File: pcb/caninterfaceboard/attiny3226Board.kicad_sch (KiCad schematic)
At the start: 78 parts, among them J1 AVR UART, J10 NTC2, J11 Attiny UDPI, J12 Flywheel, J13 1Wire, J2 CAN, J3 AVR ISP, J4 NTC3, J5 12V In, J6 FuelLevel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

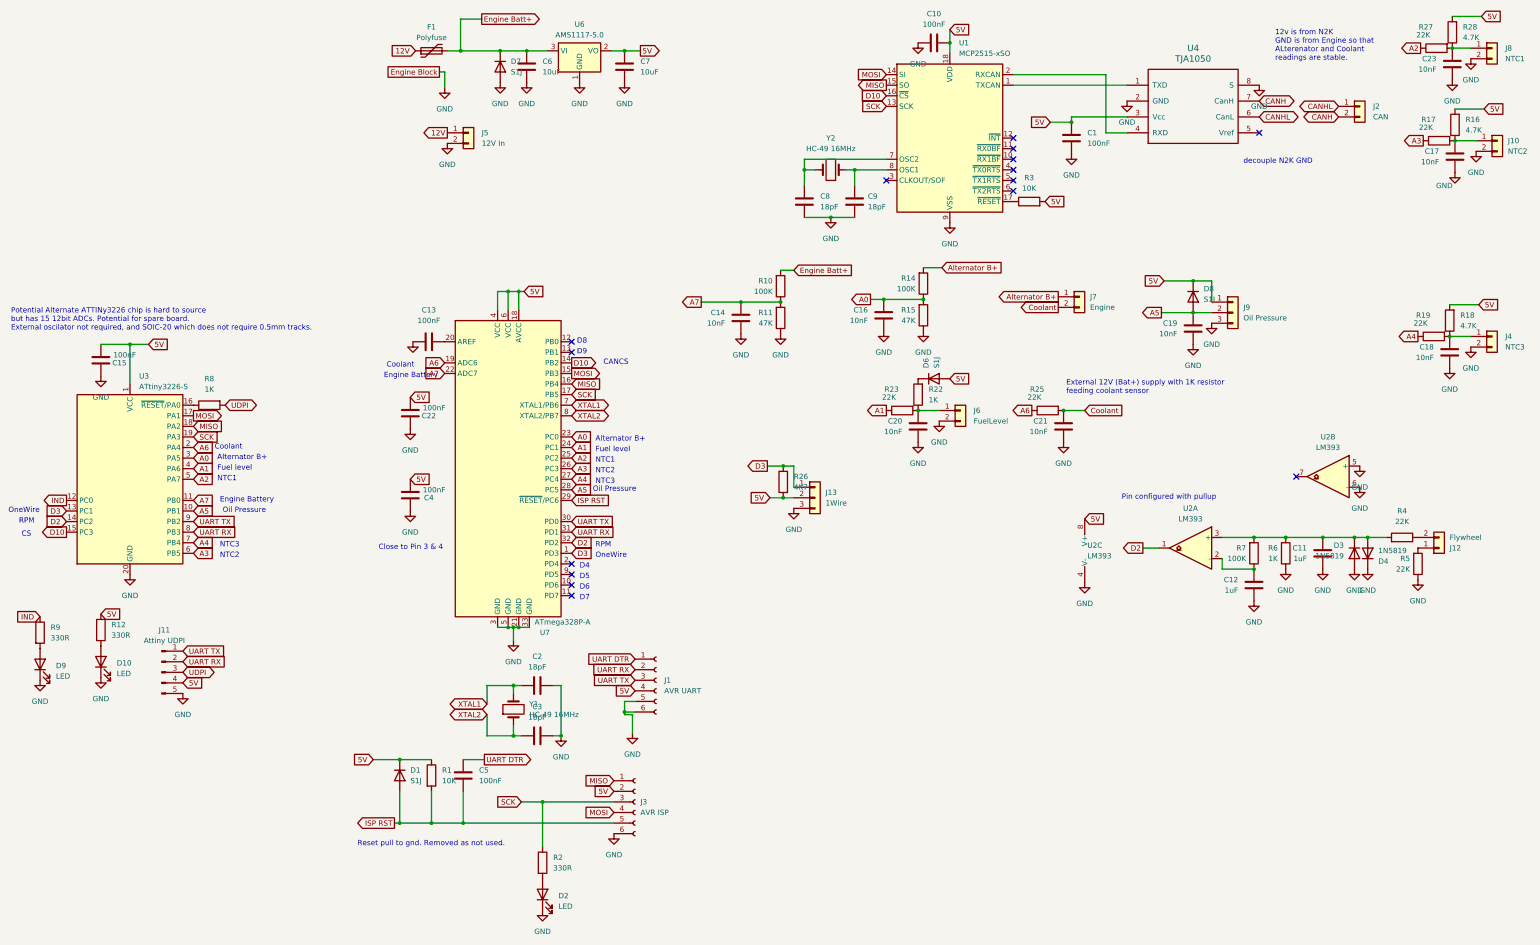
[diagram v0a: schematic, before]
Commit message: Added a attiny3226 veresion for better ADC accuracy
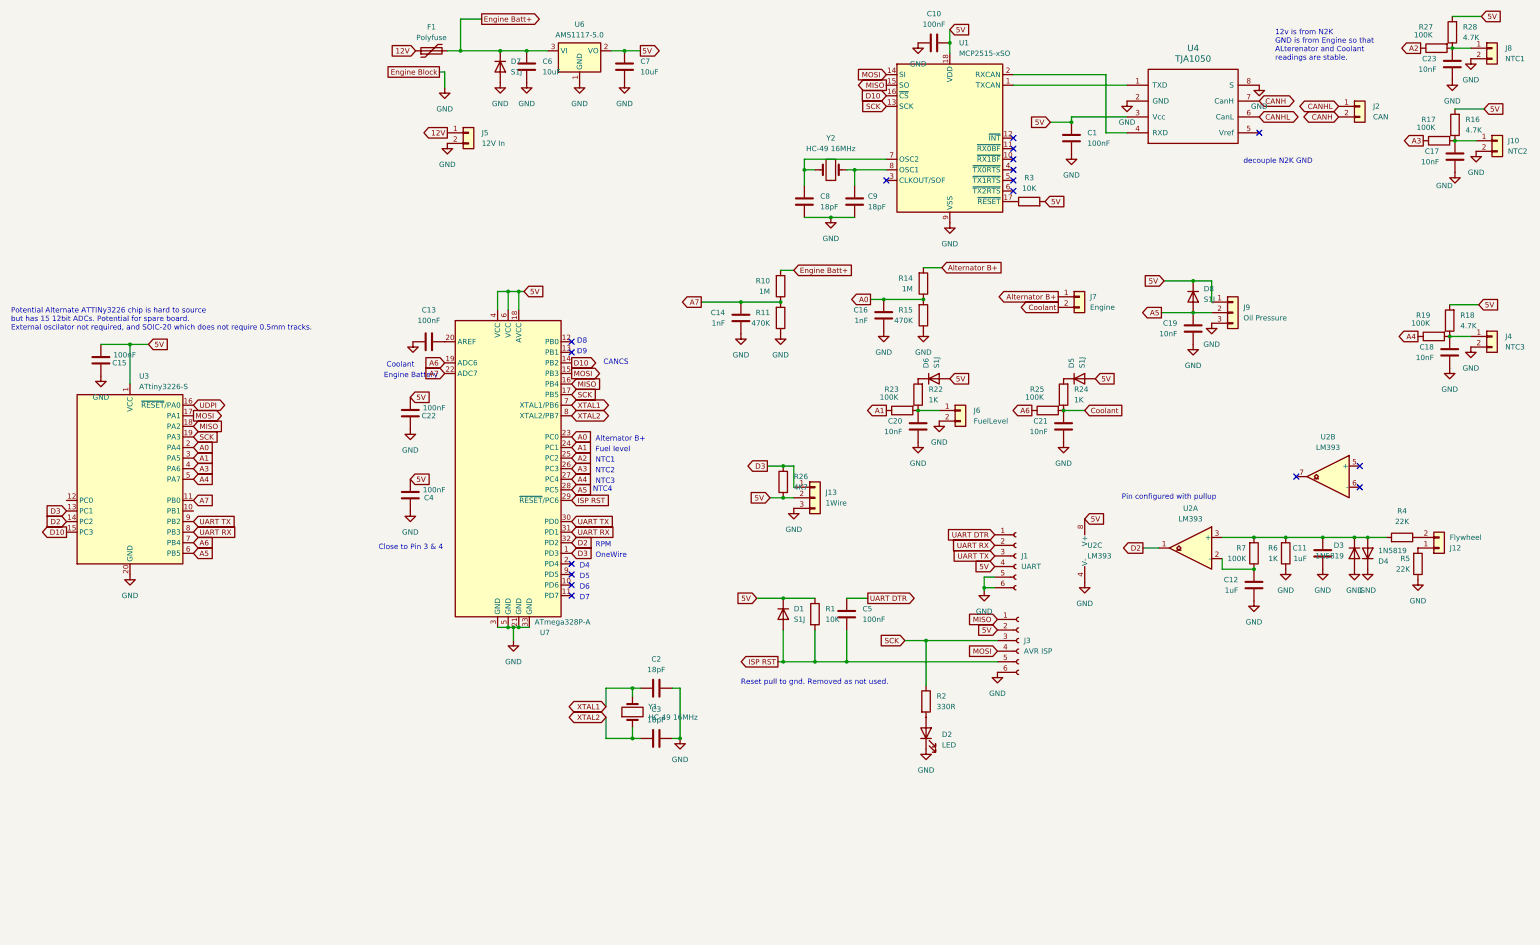
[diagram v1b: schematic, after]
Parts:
- removed D10, D9: LED, LED_SMD:LED_0805_2012Metric_Pad1.15x1.40mm_HandSolder, symbol Device:LED
- removed J11: Attiny UDPI, Connector_PinHeader_2.54mm:PinHeader_1x05_P2.54mm_Vertical, symbol Connector:Conn_01x05_Pin
- removed R12, R9: 330R, Resistor_SMD:R_0805_2012Metric_Pad1.20x1.40mm_HandSolder, symbol Device:R
- removed R8: 1K, Resistor_SMD:R_0805_2012Metric_Pad1.20x1.40mm_HandSolder, symbol Device:R
- added D5: S1J, Diode_SMD:D_0805_2012Metric_Pad1.15x1.40mm_HandSolder, symbol Device:D
- added R24: 1K, Resistor_SMD:R_0805_2012Metric_Pad1.20x1.40mm_HandSolder, symbol Device:R
- C14, C16: value 10nF -> 1nF
- J1: value AVR UART -> UART
- R10, R14: value 100K -> 1M
- R11, R15: value 47K -> 470K
- R17, R19, R23, R25, R27: value 22K -> 100K
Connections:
- net 5V: now also D5.2 (A)
- net A0: now also U3.2 (PA4); no longer U3.3 (PA5)
- net A1: now also U3.3 (PA5); no longer U3.4 (PA6)
- net A2: no longer U3.5 (PA7)
- net A3: now also U3.4 (PA6); no longer U3.6 (PB5)
- net A4: now also U3.5 (PA7); no longer U3.7 (PB4)
- net A5: now also U3.6 (PB5); no longer U3.10 (PB1)
- net A6: now also U3.7 (PB4); no longer U3.2 (PA4)
- net Coolant: now also R24.1
- net GND: no longer U2.5 (+), U2.6 (-)
- net UDPI: now also U3.16 (~{RESET}/PA0)
- net IND: no longer names the net of U3.12 (PC0)
- new net: D5.1 (K), R24.2
- no-connect marks 15 -> 17
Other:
- note added: "NTC4"
- note removed: "CS"
- note removed: "External 12V (Bat+) supply with 1K resistor feeding coolant sensor"
- note removed: "Oil Pressure"
- moved on the sheet: C2, C3, C5, D1, D2, J1, J3, R1, R2, Y1

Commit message: Finally mare the RPM to pulse amp stable
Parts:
- added C24: 100nF, Capacitor_SMD:C_0805_2012Metric_Pad1.18x1.45mm_HandSolder, symbol Device:C
- added R9: 10K, Resistor_SMD:R_0805_2012Metric_Pad1.20x1.40mm_HandSolder, symbol Device:R
- C11: value 1uF -> 470nF
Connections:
- net 5V: now also C24.2, R9.2
- net D2: now also R9.1
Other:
- note added: "Decoupling must be close to the LM393"
- note removed: "Pin configured with pullup"

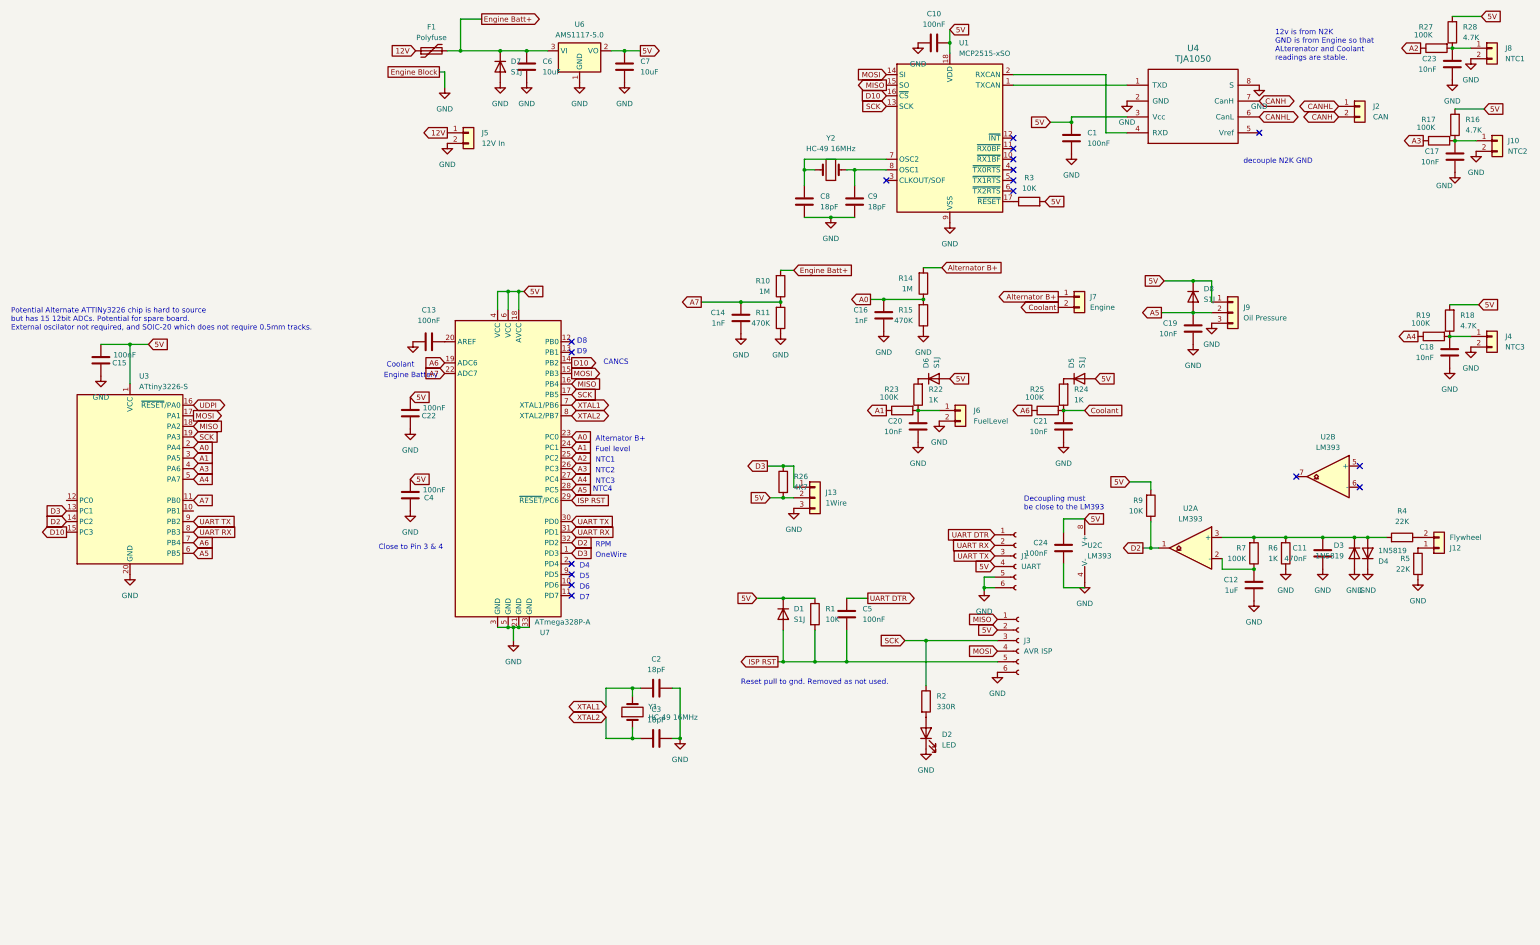
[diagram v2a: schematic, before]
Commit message: Improved flywheel detection circuit
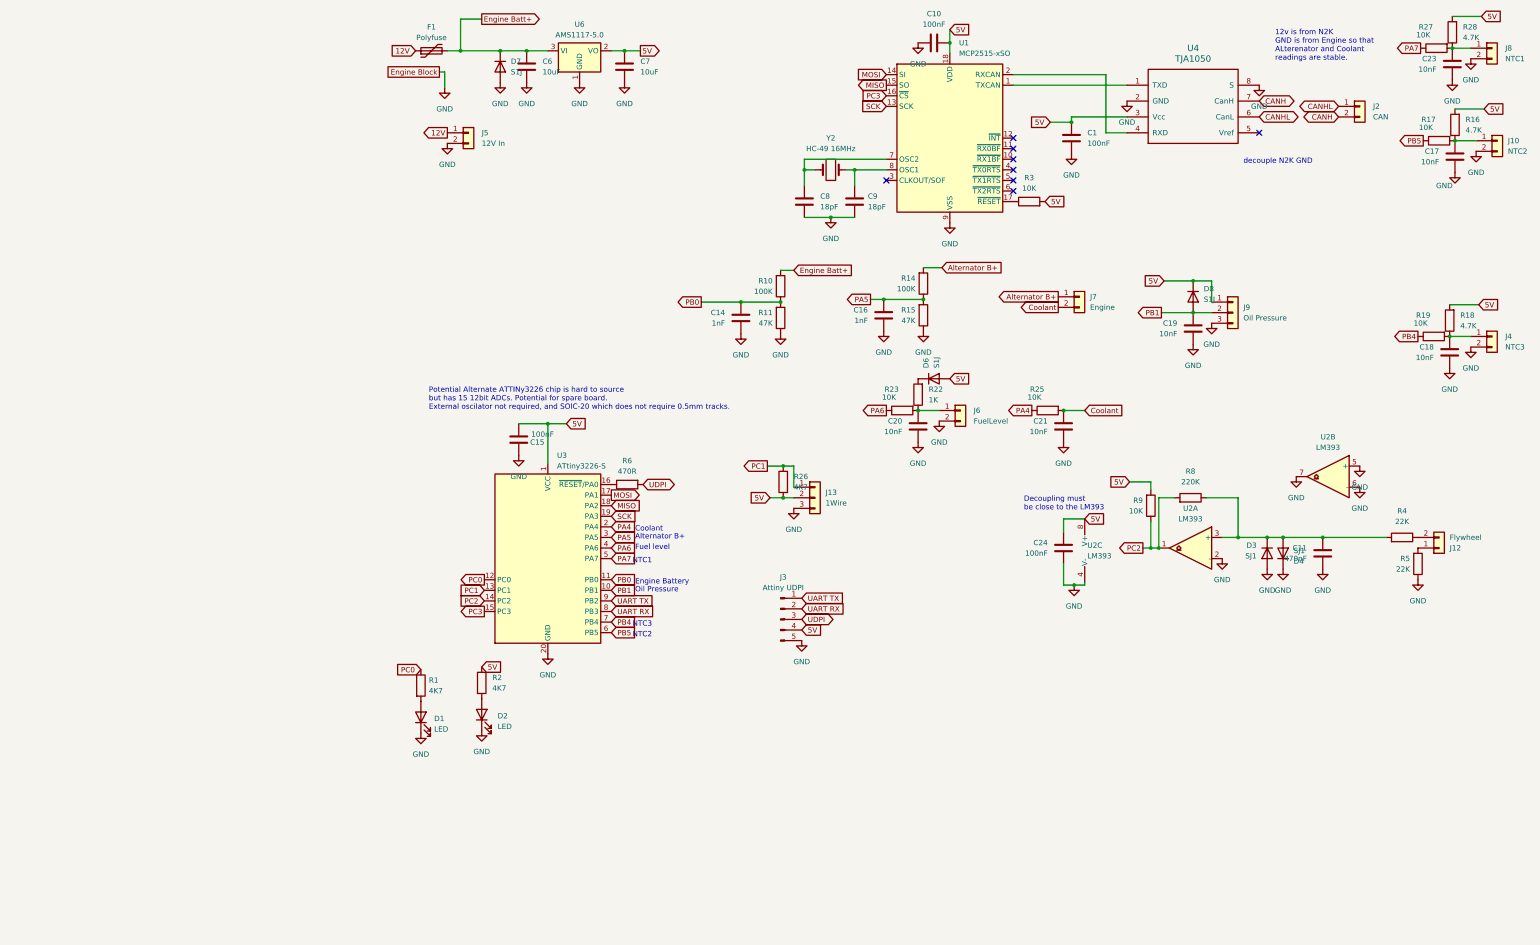
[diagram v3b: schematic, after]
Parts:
- removed C12: 1uF, Capacitor_SMD:C_0805_2012Metric_Pad1.18x1.45mm_HandSolder, symbol Device:C
- removed C13, C22, C4, C5: 100nF, Capacitor_SMD:C_0805_2012Metric_Pad1.18x1.45mm_HandSolder, symbol Device:C
- removed C2, C3: 18pF, Capacitor_SMD:C_0805_2012Metric_Pad1.18x1.45mm_HandSolder, symbol Device:C
- removed D1, D5: S1J, Diode_SMD:D_0805_2012Metric_Pad1.15x1.40mm_HandSolder, symbol Device:D
- removed J1: UART, Connector_PinSocket_2.54mm:PinSocket_1x06_P2.54mm_Vertical, symbol Connector:Conn_01x06_Socket
- removed J3: AVR ISP, Connector_PinHeader_2.54mm:PinHeader_2x03_P2.54mm_Vertical, symbol Connector:Conn_01x06_Socket
- removed R24: 1K, Resistor_SMD:R_0805_2012Metric_Pad1.20x1.40mm_HandSolder, symbol Device:R
- removed R7: 100K, Resistor_SMD:R_0805_2012Metric_Pad1.20x1.40mm_HandSolder, symbol Device:R
- removed U7: ATmega328P-A, Package_QFP:TQFP-32_7x7mm_P0.8mm, symbol MCU_Microchip_ATmega:ATmega328P-A
- removed Y1: HC-49 16MHz, Crystal:Crystal_SMD_HC49-SD, symbol Device:Crystal
- added D1: LED, LED_SMD:LED_0805_2012Metric_Pad1.15x1.40mm_HandSolder, symbol Device:LED
- added J3: Attiny UDPI, Connector_PinHeader_2.54mm:PinHeader_1x05_P2.54mm_Vertical, symbol Connector:Conn_01x05_Pin
- added R8: 220K, Resistor_SMD:R_0805_2012Metric_Pad1.20x1.40mm_HandSolder, symbol Device:R
- D3, D4: value 1N5819 -> SJ1
- R1: value 10K -> 4K7
- R10, R14: value 1M -> 100K
- R11, R15: value 470K -> 47K
- R17, R19, R23, R25, R27: value 100K -> 10K
- R2: value 330R -> 4K7
- R6: value 1K -> 470R
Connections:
- net 5V: now also R2.1, J3.4 (Pin_4); no longer R1.1
- net GND: now also C24.1, U2.2 (-), U2.5 (+), U2.6 (-), U2.7, D1.1 (K), J3.5 (Pin_5); no longer R6.1
- net SCK: no longer R2.1
- net UART RX: now also J3.2 (Pin_2)
- net UART TX: now also J3.1 (Pin_1)
- net UDPI: now also R6.2, J3.3 (Pin_3); no longer U3.16 (~{RESET}/PA0)
- net at C11.2, D3.1 (K), D4.2 (A)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: now also R8.1; no longer R6.2
- net PB1: now reaches U3.10 (PB1)
- net PB1: now also C19.2, D8.2 (A), J9.2 (Pin_2)
- net PC0: now reaches U3.12 (PC0)
- net PC0: now also R1.1
- net A0 renamed PA5
- net PA5: now also U3.3 (PA5); no longer U3.2 (PA4)
- net A1 renamed PA6
- net PA6: now also U3.4 (PA6); no longer U3.3 (PA5)
- net A2 renamed PA7
- net PA7: now also U3.5 (PA7)
- net A3 renamed PB5
- net PB5: now also U3.6 (PB5); no longer U3.4 (PA6)
- net A4 renamed PB4
- net PB4: now also U3.7 (PB4); no longer U3.5 (PA7)
- removed net A5: C19.2, D8.2 (A), J9.2 (Pin_2), U3.6 (PB5)
- net A6 renamed PA4
- net PA4: now also U3.2 (PA4); no longer U3.7 (PB4)
- net A7 renamed PB0
- net D10 renamed PC3
- net D2 renamed PC2
- net PC2: now also R8.2
- net D3 renamed PC1
- net ISP RST: no longer names the net of R1.2
- net ISP RST: now also D1.2 (A)
- new net: R6.1, U3.16 (~{RESET}/PA0)
- no-connect marks 17 -> 8
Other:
- note added: "Oil Pressure"
- note removed: "CANCS"
- note removed: "Close to Pin 3 & 4"
- note removed: "D4"
- note removed: "D5"
- note removed: "D6"
- note removed: "D7"
- note removed: "D8"
- note removed: "D9"
- note removed: "NTC4"
- note removed: "OneWire"
- note removed: "RPM"
- note removed: "Reset pull to gnd. Removed as not used."
- moved on the sheet: C15, D3, D4, U3
